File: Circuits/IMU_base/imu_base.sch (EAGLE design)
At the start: 11 parts, among them U1 LSM9DS1

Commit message: connected 6 conn package and symbol, base board layout complete
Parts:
- added R1: 10k, SparkFun-Resistors:10KOHM-0603-1/10W-1%
- U$2: value MOLEX_522070433 -> MOLEX_522070633; device custom:MOLEX_522070433 -> custom:MOLEX_522070633
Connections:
- new net SA0: R1.1, U1.SDO_A/G
- new net SCL1: U$2.5, U1.SCL/SPC
- new net SDA1: U$2.6, U1.SDA/SDI/SDO
- net GND: now also U$1.2, U$2.3; no longer U$1.3, U$2.2, U1.SDO_A/G
- net SCL: now also U$1.4, U$2.1; no longer U$1.1, U$2.4, U1.SCL/SPC
- net SDA: now also U$1.3, U$2.2; no longer U$1.2, U$2.3, U1.SDA/SDI/SDO
- net VCC: now also R1.2, U$1.1, U$2.4; no longer U$1.4, U$2.1
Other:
- note removed: "SDO_A/G, aka SA0, grounded to set I2C address"
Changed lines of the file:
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@@
 <part name="R4" library="SparkFun-Resistors" deviceset="10KOHM" device="-0603-1/10W-1%" value="10k"/>
 <part name="U$1" library="custom" deviceset="MOLEX_522070433" device=""/>
-<part name="U$2" library="custom" deviceset="MOLEX_522070433" device=""/>
-<part name="GND7" library="SparkFun-PowerSymbols" deviceset="GND" device=""/>
+<part name="R1" library="SparkFun-Resistors" deviceset="10KOHM" device="-0603-1/10W-1%" value="10k"/>
+<part name="SUPPLY3" library="SparkFun-PowerSymbols" deviceset="VCC" device=""/>
+<part name="U$2" library="custom" deviceset="MOLEX_522070633" device="" value="MOLEX_522070633"/>
 </parts>
 <sheets>
 <sheet>
 <plain>
-<text x="91.44" y="48.26" size="1.778" layer="91">SDO_A/G, aka SA0, grounded to set I2C address</text>
 </plain>
 <instances>
@@
 <attribute name="VALUE" x="53.33661875" y="96.5116" size="1.779190625" layer="96"/>
 </instance>
-<instance part="U$2" gate="G$1" x="60.96" y="25.4" smashed="yes">
-<attribute name="NAME" x="55.869140625" y="34.054459375" size="1.781809375" layer="95"/>
-<attribute name="VALUE" x="55.87661875" y="17.7716" size="1.779190625" layer="96"/>
-</instance>
-<instance part="GND7" gate="1" x="101.6" y="76.2" smashed="yes">
-<attribute name="VALUE" x="101.6" y="75.946" size="1.778" layer="96" align="top-center"/>
+<instance part="R1" gate="G$1" x="99.06" y="81.28" smashed="yes" rot="R90">
+<attribute name="NAME" x="97.536" y="81.28" size="1.778" layer="95" font="vector" rot="R90" align="bottom-center"/>
+<attribute name="VALUE" x="100.584" y="81.28" size="1.778" layer="96" font="vector" rot="R90" align="top-center"/>
+</instance>
+<instance part="SUPPLY3" gate="G$1" x="99.06" y="91.44" smashed="yes">
+<attribute name="VALUE" x="99.06" y="94.234" size="1.778" layer="96" align="bottom-center"/>
+</instance>
+<instance part="U$2" gate="G$1" x="58.42" y="22.86" smashed="yes">
+<attribute name="NAME" x="53.34" y="33.02" size="1.778" layer="95"/>
+<attribute name="VALUE" x="53.34" y="12.7" size="1.778" layer="96"/>
 </instance>
 </instances>
@@
 </segment>
 <segment>
-<wire x1="68.58" y1="104.14" x2="73.66" y2="104.14" width="0.1524" layer="91"/>
-<label x="68.58" y="104.14" size="1.778" layer="95"/>
-<pinref part="U$1" gate="G$1" pin="3"/>
-</segment>
-<segment>
-<pinref part="U1" gate="G$1" pin="SDO_A/G"/>
-<wire x1="81.28" y1="73.66" x2="99.06" y2="73.66" width="0.1524" layer="91"/>
-<wire x1="99.06" y1="73.66" x2="99.06" y2="81.28" width="0.1524" layer="91"/>
-<wire x1="99.06" y1="81.28" x2="101.6" y2="81.28" width="0.1524" layer="91"/>
-<wire x1="101.6" y1="81.28" x2="101.6" y2="78.74" width="0.1524" layer="91"/>
-<pinref part="GND7" gate="1" pin="GND"/>
-</segment>
-<segment>
-<pinref part="U$2" gate="G$1" pin="2"/>
-<wire x1="71.12" y1="27.94" x2="78.74" y2="27.94" width="0.1524" layer="91"/>
-<label x="73.66" y="27.94" size="1.778" layer="95"/>
+<pinref part="U$1" gate="G$1" pin="2"/>
+<wire x1="68.58" y1="106.68" x2="73.66" y2="106.68" width="0.1524" layer="91"/>
+<label x="68.58" y="106.68" size="1.778" layer="95"/>
+</segment>
+<segment>
+<pinref part="U$2" gate="G$1" pin="3"/>
+<wire x1="68.58" y1="25.4" x2="73.66" y2="25.4" width="0.1524" layer="91"/>
+<label x="68.58" y="25.4" size="1.778" layer="95"/>
 </segment>
 </net>
@@
 </segment>
 <segment>
-<wire x1="68.58" y1="101.6" x2="73.66" y2="101.6" width="0.1524" layer="91"/>
-<label x="68.58" y="101.6" size="1.778" layer="95"/>
-<pinref part="U$1" gate="G$1" pin="4"/>
-</segment>
-<segment>
-<pinref part="U$2" gate="G$1" pin="1"/>
-<wire x1="71.12" y1="30.48" x2="78.74" y2="30.48" width="0.1524" layer="91"/>
-<label x="73.66" y="30.48" size="1.778" layer="95"/>
+<pinref part="R1" gate="G$1" pin="2"/>
+<pinref part="SUPPLY3" gate="G$1" pin="VCC"/>
+<wire x1="99.06" y1="86.36" x2="99.06" y2="91.44" width="0.1524" layer="91"/>
+</segment>
+<segment>
+<pinref part="U$1" gate="G$1" pin="1"/>
+<wire x1="68.58" y1="109.22" x2="73.66" y2="109.22" width="0.1524" layer="91"/>
+<label x="68.58" y="109.22" size="1.778" layer="95"/>
+</segment>
+<segment>
+<pinref part="U$2" gate="G$1" pin="4"/>
+<wire x1="68.58" y1="22.86" x2="73.66" y2="22.86" width="0.1524" layer="91"/>
+<label x="68.58" y="22.86" size="1.778" layer="95"/>
 </segment>
 </net>
@@
 </segment>
 </net>
+<net name="SA0" class="0">
+<segment>
+<pinref part="U1" gate="G$1" pin="SDO_A/G"/>
+<wire x1="81.28" y1="73.66" x2="99.06" y2="73.66" width="0.1524" layer="91"/>
+<pinref part="R1" gate="G$1" pin="1"/>
+<wire x1="99.06" y1="76.2" x2="99.06" y2="73.66" width="0.1524" layer="91"/>
+<label x="83.82" y="73.66" size="1.778" layer="95"/>
+</segment>
+</net>
 <net name="SDA" class="0">
 <segment>
+<pinref part="U$1" gate="G$1" pin="3"/>
+<wire x1="68.58" y1="104.14" x2="73.66" y2="104.14" width="0.1524" layer="91"/>
+<label x="68.58" y="104.14" size="1.778" layer="95"/>
+</segment>
+<segment>
+<pinref part="U$2" gate="G$1" pin="2"/>
+<wire x1="68.58" y1="27.94" x2="73.66" y2="27.94" width="0.1524" layer="91"/>
+<label x="68.58" y="27.94" size="1.778" layer="95"/>
+</segment>
+</net>
+<net name="SCL" class="0">
+<segment>
+<pinref part="U$1" gate="G$1" pin="4"/>
+<wire x1="68.58" y1="101.6" x2="73.66" y2="101.6" width="0.1524" layer="91"/>
+<label x="68.58" y="101.6" size="1.778" layer="95"/>
+</segment>
+<segment>
+<pinref part="U$2" gate="G$1" pin="1"/>
+<wire x1="68.58" y1="30.48" x2="73.66" y2="30.48" width="0.1524" layer="91"/>
+<label x="68.58" y="30.48" size="1.778" layer="95"/>
+</segment>
+</net>
+<net name="SDA1" class="0">
+<segment>
 <pinref part="U1" gate="G$1" pin="SDA/SDI/SDO"/>
-<wire x1="81.28" y1="78.74" x2="83.82" y2="78.74" width="0.1524" layer="91"/>
-<label x="83.82" y="78.74" size="1.778" layer="95"/>
-</segment>
-<segment>
-<wire x1="68.58" y1="106.68" x2="73.66" y2="106.68" width="0.1524" layer="91"/>
-<label x="68.58" y="106.68" size="1.778" layer="95"/>
-<pinref part="U$1" gate="G$1" pin="2"/>
-</segment>
-<segment>
-<pinref part="U$2" gate="G$1" pin="3"/>
-<wire x1="71.12" y1="25.4" x2="78.74" y2="25.4" width="0.1524" layer="91"/>
-<label x="73.66" y="25.4" size="1.778" layer="95"/>
-</segment>
-</net>
-<net name="SCL" class="0">
+<wire x1="81.28" y1="78.74" x2="86.36" y2="78.74" width="0.1524" layer="91"/>
+<label x="81.28" y="78.74" size="1.778" layer="95"/>
+</segment>
+<segment>
+<pinref part="U$2" gate="G$1" pin="6"/>
+<wire x1="68.58" y1="17.78" x2="73.66" y2="17.78" width="0.1524" layer="91"/>
+<label x="68.58" y="17.78" size="1.778" layer="95"/>
+</segment>
+</net>
+<net name="SCL1" class="0">
 <segment>
 <pinref part="U1" gate="G$1" pin="SCL/SPC"/>
-<wire x1="81.28" y1="76.2" x2="83.82" y2="76.2" width="0.1524" layer="91"/>
-<label x="83.82" y="76.2" size="1.778" layer="95"/>
-</segment>
-<segment>
-<pinref part="U$2" gate="G$1" pin="4"/>
-<wire x1="71.12" y1="22.86" x2="73.66" y2="22.86" width="0.1524" layer="91"/>
-<label x="73.66" y="22.86" size="1.778" layer="95"/>
-</segment>
-<segment>
-<pinref part="U$1" gate="G$1" pin="1"/>
-<wire x1="68.58" y1="109.22" x2="73.66" y2="109.22" width="0.1524" layer="91"/>
-<label x="68.58" y="109.22" size="1.778" layer="95"/>
-</segment>
-</net>
+<wire x1="81.28" y1="76.2" x2="86.36" y2="76.2" width="0.1524" layer="91"/>
+<label x="81.28" y="76.2" size="1.778" layer="95"/>
+</segment>
+<segment>
+<pinref part="U$2" gate="G$1" pin="5"/>
+<wire x1="68.58" y1="20.32" x2="73.66" y2="20.32" width="0.1524" layer="91"/>
+<label x="68.58" y="20.32" size="1.778" layer="95"/>
+</segment>
+</net>

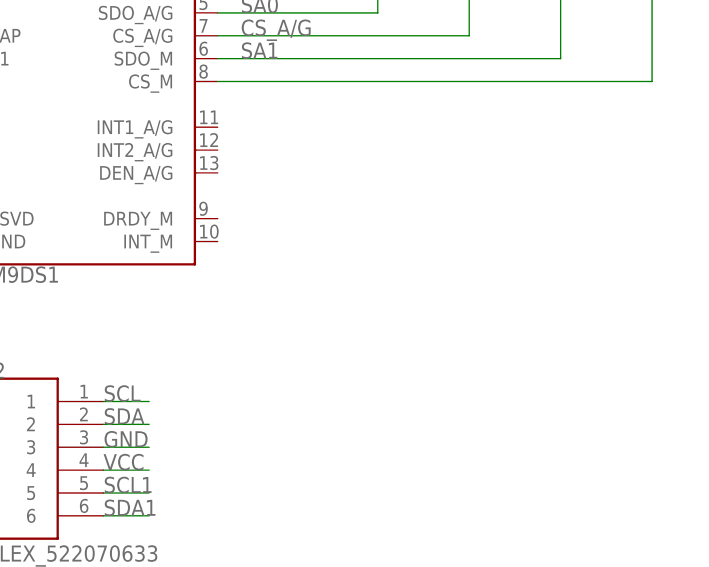
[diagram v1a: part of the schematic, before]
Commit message: Added testpad in schematic and board layout to allow address to be pulled up or down when needed
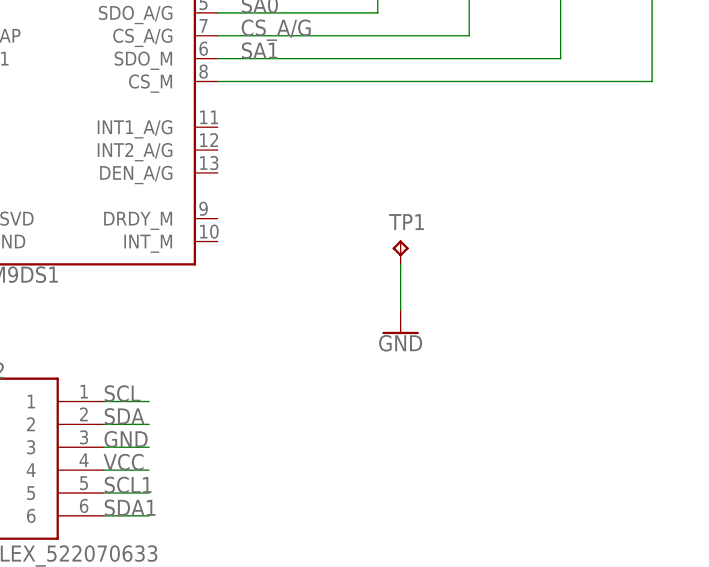
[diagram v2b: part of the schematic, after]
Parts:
- added TP1: TPB1,27, testpad:TPB1,27
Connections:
- net GND: now also TP1.TP
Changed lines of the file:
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@@
 <part name="SUPPLY3" library="SparkFun-PowerSymbols" deviceset="VCC" device=""/>
 <part name="U$2" library="custom" deviceset="MOLEX_522070633" device="" value="MOLEX_522070633"/>
+<part name="TP1" library="testpad" library_urn="urn:adsk.eagle:library:385" deviceset="TP" device="B1,27" package3d_urn="urn:adsk.eagle:package:27944/2"/>
+<part name="GND7" library="SparkFun-PowerSymbols" deviceset="GND" device=""/>
 </parts>
 <sheets>
@@
 <attribute name="VALUE" x="53.34" y="12.7" size="1.778" layer="96"/>
 </instance>
+<instance part="TP1" gate="G$1" x="101.6" y="48.26" smashed="yes">
+<attribute name="NAME" x="100.33" y="49.53" size="1.778" layer="95"/>
+<attribute name="TP_SIGNAL_NAME" x="102.87" y="46.99" size="1.778" layer="97"/>
+</instance>
+<instance part="GND7" gate="1" x="101.6" y="38.1" smashed="yes">
+<attribute name="VALUE" x="101.6" y="37.846" size="1.778" layer="96" align="top-center"/>
+</instance>
 </instances>
 <busses>
@@
 <wire x1="68.58" y1="25.4" x2="73.66" y2="25.4" width="0.1524" layer="91"/>
 <label x="68.58" y="25.4" size="1.778" layer="95"/>
+</segment>
+<segment>
+<pinref part="TP1" gate="G$1" pin="TP"/>
+<pinref part="GND7" gate="1" pin="GND"/>
+<wire x1="101.6" y1="45.72" x2="101.6" y2="40.64" width="0.1524" layer="91"/>
 </segment>
 </net>
@@
 </schematic>
 </drawing>
+<compatibility>
+<note version="8.2" severity="warning">
+Since Version 8.2, EAGLE supports online libraries. The ids
+of those online libraries will not be understood (or retained)
+with this version.
+</note>
+<note version="8.3" severity="warning">
+Since Version 8.3, EAGLE supports URNs for individual library
+assets (packages, symbols, and devices). The URNs of those assets
+will not be understood (or retained) with this version.
+</note>
+<note version="8.3" severity="warning">
+Since Version 8.3, EAGLE supports the association of 3D packages
+with devices in libraries, schematics, and board files. Those 3D
+packages will not be understood (or retained) with this version.
+</note>
+</compatibility>
 </eagle>

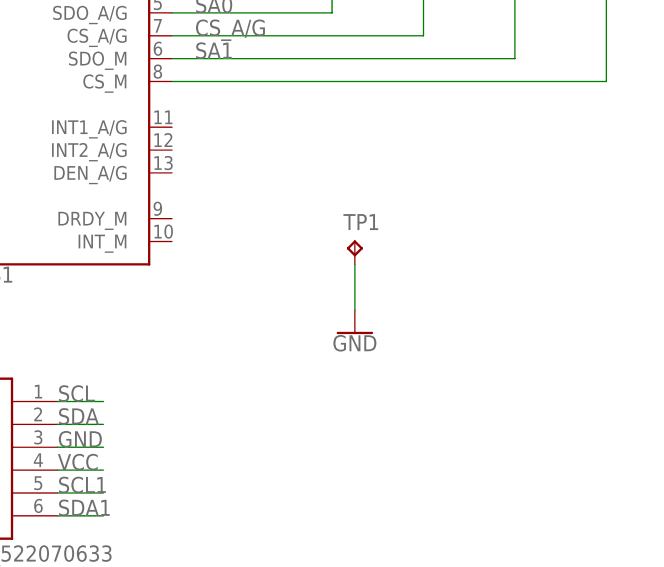
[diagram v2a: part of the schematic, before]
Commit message: change test pad size up
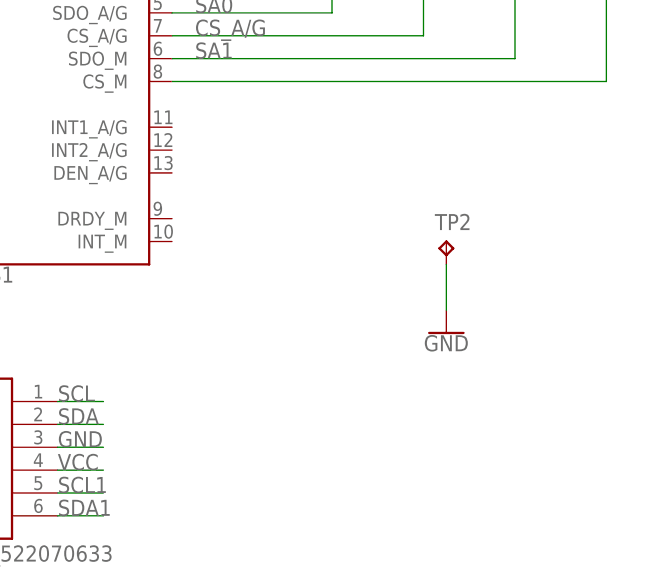
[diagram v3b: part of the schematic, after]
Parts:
- removed TP1: TPB1,27, testpad:TPB1,27
- added TP2: TPB2,54, testpad:TPB2,54
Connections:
- net GND: now also TP2.TP; no longer TP1.TP
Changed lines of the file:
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@@
 <part name="SUPPLY3" library="SparkFun-PowerSymbols" deviceset="VCC" device=""/>
 <part name="U$2" library="custom" deviceset="MOLEX_522070633" device="" value="MOLEX_522070633"/>
-<part name="TP1" library="testpad" library_urn="urn:adsk.eagle:library:385" deviceset="TP" device="B1,27" package3d_urn="urn:adsk.eagle:package:27944/2"/>
 <part name="GND7" library="SparkFun-PowerSymbols" deviceset="GND" device=""/>
+<part name="TP2" library="testpad" library_urn="urn:adsk.eagle:library:385" deviceset="TP" device="B2,54" package3d_urn="urn:adsk.eagle:package:27948/1"/>
 </parts>
 <sheets>
@@
 <attribute name="VALUE" x="53.34" y="12.7" size="1.778" layer="96"/>
 </instance>
-<instance part="TP1" gate="G$1" x="101.6" y="48.26" smashed="yes">
-<attribute name="NAME" x="100.33" y="49.53" size="1.778" layer="95"/>
-<attribute name="TP_SIGNAL_NAME" x="102.87" y="46.99" size="1.778" layer="97"/>
+<instance part="GND7" gate="1" x="111.76" y="38.1" smashed="yes">
+<attribute name="VALUE" x="111.76" y="37.846" size="1.778" layer="96" align="top-center"/>
 </instance>
-<instance part="GND7" gate="1" x="101.6" y="38.1" smashed="yes">
-<attribute name="VALUE" x="101.6" y="37.846" size="1.778" layer="96" align="top-center"/>
+<instance part="TP2" gate="G$1" x="111.76" y="48.26" smashed="yes">
+<attribute name="NAME" x="110.49" y="49.53" size="1.778" layer="95"/>
+<attribute name="TP_SIGNAL_NAME" x="113.03" y="46.99" size="1.778" layer="97"/>
 </instance>
 </instances>
@@
 </segment>
 <segment>
-<pinref part="TP1" gate="G$1" pin="TP"/>
+<pinref part="TP2" gate="G$1" pin="TP"/>
 <pinref part="GND7" gate="1" pin="GND"/>
-<wire x1="101.6" y1="45.72" x2="101.6" y2="40.64" width="0.1524" layer="91"/>
+<wire x1="111.76" y1="45.72" x2="111.76" y2="40.64" width="0.1524" layer="91"/>
 </segment>
 </net>
